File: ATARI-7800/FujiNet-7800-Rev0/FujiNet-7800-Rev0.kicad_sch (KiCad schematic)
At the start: 0 parts

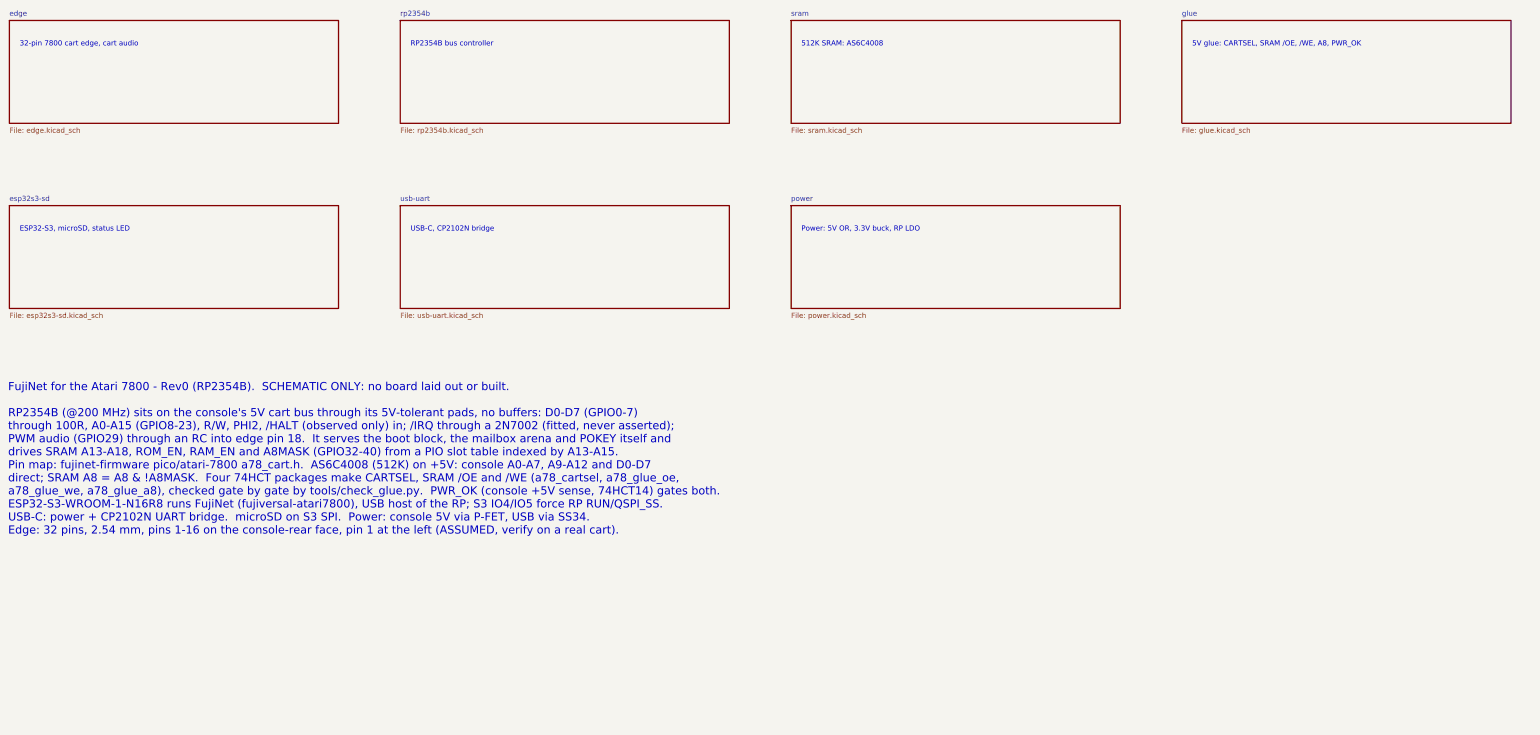
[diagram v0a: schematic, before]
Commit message: ATARI-7800 Rev0: fix the edge, audit the circuit, redraw from the slot, place the board
Edge (board-killer in the schematic-only footprint): the 7800 edge has 18
positions at 2.54 mm with key slots at 3 and 16 for the console's plastic
keys. Pins 1, 2, 15, 16 (and 32, 31, 18, 17) sat one pitch inward, on the
key positions, with no slots and a 42.6 mm tab. tools/edge_geom.py now holds
the geometry (47.0 mm tab, slots centred on +-16.51, 2.4 x 10 mm);
tools/audit/edge_orientation.py checks it against Otaku-flash, tdididit's
boards, the a78-devcart gerbers and this repo's working FujiPlusCart
prototype gerbers (faces and power fingers).

Circuit (console research: Atari C025231 schematic, GCC1702B MARIA spec):
- 4.7k pull-downs on ROM_EN / RAM_EN / A8MASK (RP2350-E9)
- 1k at the /HALT finger (MARIA's HALT is a weak MOS output)
- 10 uF at the console 5V finger; bring-up test pads
- TS-1187A buttons and WS2812C-2020-V1 (the TL3342 and WS2812B-2020
  had 5 in stock at JLC); manufacturer fields for PCBWay
No glue change: R/W is pulled up during MARIA DMA, and the console gates
A15/A14/A12 low while its BIOS is mapped, so CARTSEL never fights it.

Schematic: SMS Rev0's hierarchy (wired root block diagram, hierarchical
labels, netlist parity); sheets in flow order from the slot; the glue
redrawn as a left-to-right gate-depth diagram; references renumbered
from the slot. ERC 0, check_nets 383/383, check_glue 4096/4096.

Board (not yet routed): SMS Rev0's 6-layer pipeline ported. A 72.4 x 115 mm
outline: the stock T-bar width on a 47 x 16.5 mm tab, with the key slots
cut in. Placement variant A (RP over the address fingers, SRAM over the
data fingers): unrouted DRC 0 errors, parity 0, check_vias 0. Shell:
case/FujiNet-7800-Shell.scad. README still describes the old board.

Co-Authored-By: Claude Opus 5.5 <noreply@anthropic.com>
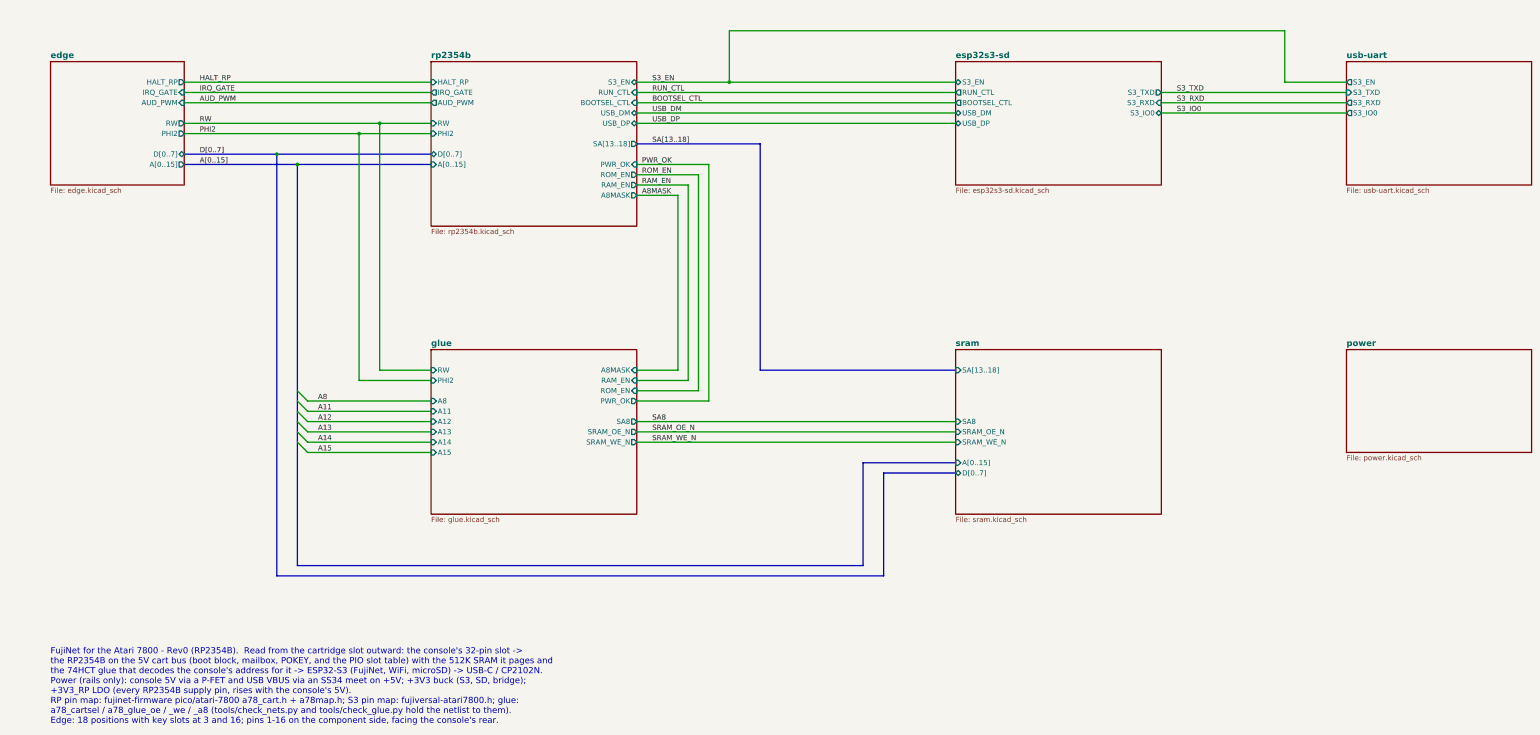
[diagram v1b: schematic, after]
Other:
- sheet edge ports: added AUD_PWM, A[0..15], D[0..7], HALT_RP, IRQ_GATE, PHI2, RW; removed none
- sheet esp32s3-sd ports: added BOOTSEL_CTL, RUN_CTL, S3_EN, S3_IO0, S3_RXD, S3_TXD, USB_DM, USB_DP; removed none
- sheet glue ports: added A11, A12, A13, A14, A15, A8, A8MASK, PHI2, PWR_OK, RAM_EN, ROM_EN, RW, SA8, SRAM_OE_N, SRAM_WE_N; removed none
- sheet rp2354b ports: added A8MASK, AUD_PWM, A[0..15], BOOTSEL_CTL, D[0..7], HALT_RP, IRQ_GATE, PHI2, PWR_OK, RAM_EN, ROM_EN, RUN_CTL, RW, S3_EN, SA[13..18], USB_DM, USB_DP; removed none
- sheet sram ports: added A[0..15], D[0..7], SA8, SA[13..18], SRAM_OE_N, SRAM_WE_N; removed none
- sheet usb-uart ports: added S3_EN, S3_IO0, S3_RXD, S3_TXD; removed none
- note added: "FujiNet for the Atari 7800 - Rev0 (RP2354B). Read from the cartridge slot outward: the console's 32-pin slot -> the RP2354B on the 5V cart bus (boot block, mailbox, POKEY, and the PIO slot table) with the 512K SRAM it pages and the 74HCT glue that decodes the console's address for it -> ESP32-S3 (FujiNet, WiFi, microSD) -> USB-C / CP2102N. Power (rails only): console 5V via a P-FET and USB VBUS v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"
- note removed: "32-pin 7800 cart edge, cart audio"
- note removed: "512K SRAM: AS6C4008"
- note removed: "5V glue: CARTSEL, SRAM /OE, /WE, A8, PWR_OK"
- note removed: "ESP32-S3, microSD, status LED"
- note removed: "FujiNet for the Atari 7800 - Rev0 (RP2354B). SCHEMATIC ONLY: no board laid out or built. RP2354B (@200 MHz) sits on the console's 5V cart bus through its 5V-tolerant pads, no buffers: D0-D7 (GPIO0-7) through 100R, A0-A15 (GPIO8-23), R/W, PHI2, /HALT (observed only) in; /IRQ through a 2N7002 (fitted, never asserted); PWM audio (GPIO29) through an RC into edge pin 18. It serves the boot block, the 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"
- note removed: "Power: 5V OR, 3.3V buck, RP LDO"
- note removed: "RP2354B bus controller"
- note removed: "USB-C, CP2102N bridge"
